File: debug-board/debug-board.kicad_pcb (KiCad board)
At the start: 2 copper layers, 29 parts, among them J14 Conn_01x02_Pin, J5 Conn_01x02_Pin, U1 AZ1117CH-3.3TRG1, U2 PIC18F47Q84-I/PT, U3 MAX3051ESA+, Y1 40MHz

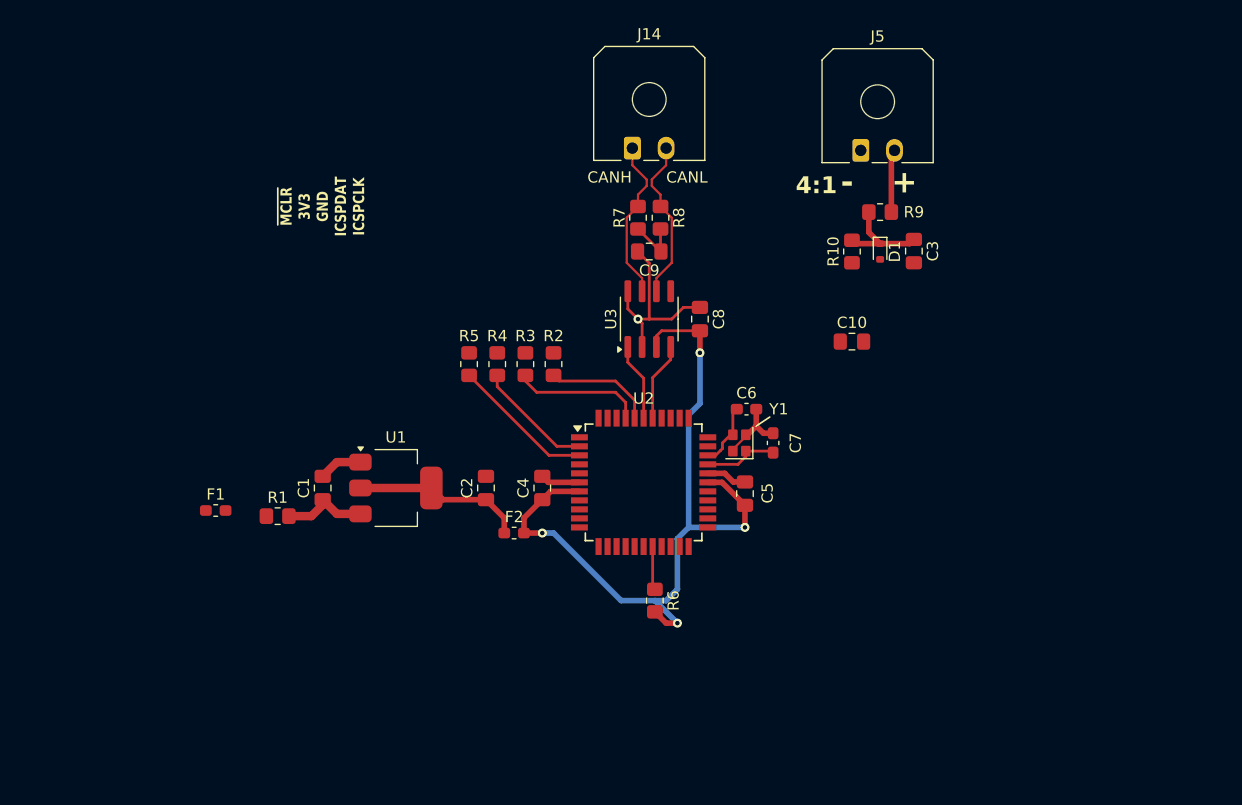
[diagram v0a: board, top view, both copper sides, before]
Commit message: Add a thermistor sensor and possibly connectors
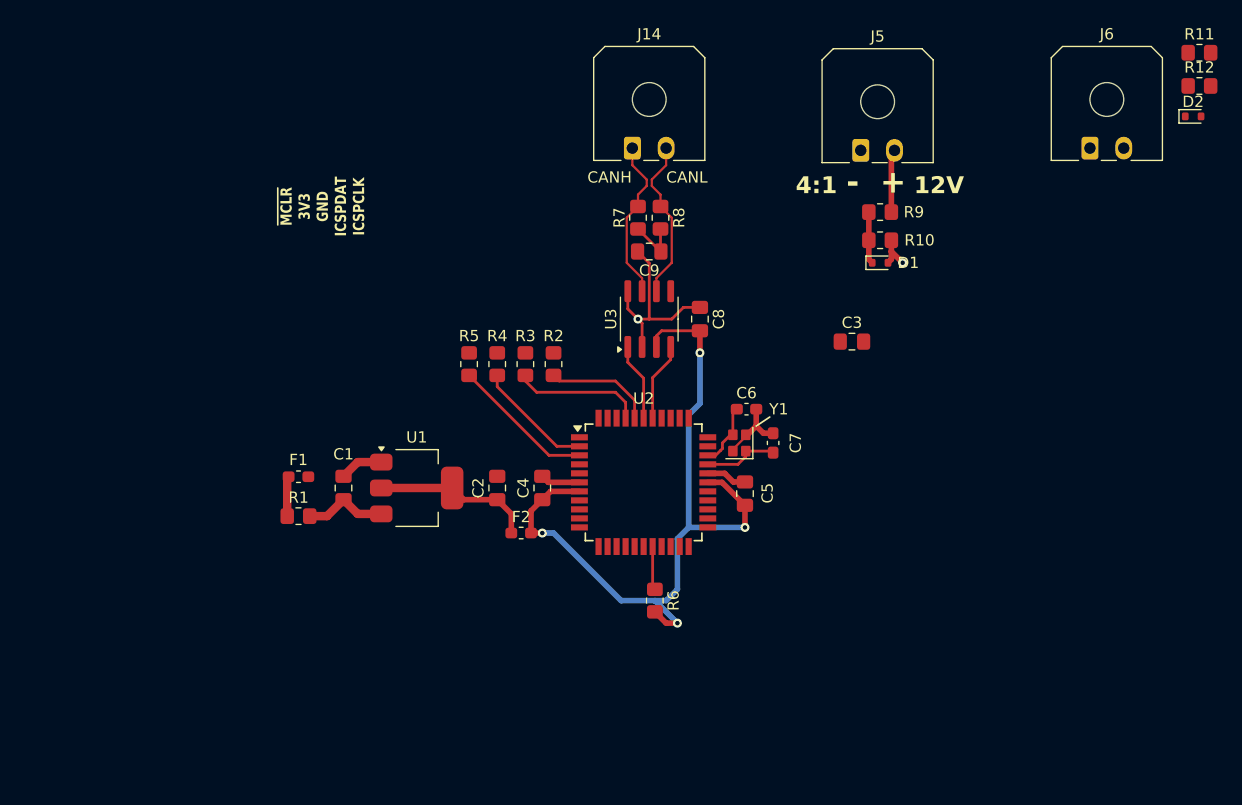
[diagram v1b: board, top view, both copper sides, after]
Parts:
- removed the C3 at (174.0, 79.5)
- added D2: BZT585B3V3T-7, Diode_SMD:D_SOD-523, F.Cu at (198.8, 67.5)
- added J6: Conn_01x02_Pin, Connector_Molex:Molex_Micro-Fit_3.0_43650-0200_1x02_P3.00mm_Horizontal, F.Cu at (189.6, 70.3)
- added R11: 40k, Resistor_SMD:R_0805_2012Metric_Pad1.20x1.40mm_HandSolder, F.Cu at (199.4, 61.9)
- added R12: 10k, Resistor_SMD:R_0805_2012Metric_Pad1.20x1.40mm_HandSolder, F.Cu at (199.4, 64.8)
- moved F1 7.94 mm to (119.3, 99.5), turned to 180 degrees
- moved R10 2.69 mm to (171.0, 78.5), turned to 180 degrees
- moved C1 1.85 mm to (123.3, 100.5)
- moved R1 1.85 mm to (119.3, 103.0)
- moved U1 1.85 mm to (129.8, 100.5)
- moved C2 1.00 mm to (137.0, 100.5)
- moved D1 1.00 mm to (171.0, 80.5), turned to 0 degrees
- moved F2 0.62 mm to (139.1, 104.5)
- renumbered C10 to C3
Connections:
- net /4:1 P/D renamed /4:1 P/D 1
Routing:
- net /4:1 P/D 1: track 8.99 -> 4.62 mm
- net Net-(F1-Pad2): track 0.00 -> 3.55 mm
- net GND: track 34.9 -> 38.5 mm, vias 1 -> 2
- net +3V3: track 68.9 -> 68.1 mm
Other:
- board text added: "12V"

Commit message: Changed footprint need to rearrange things
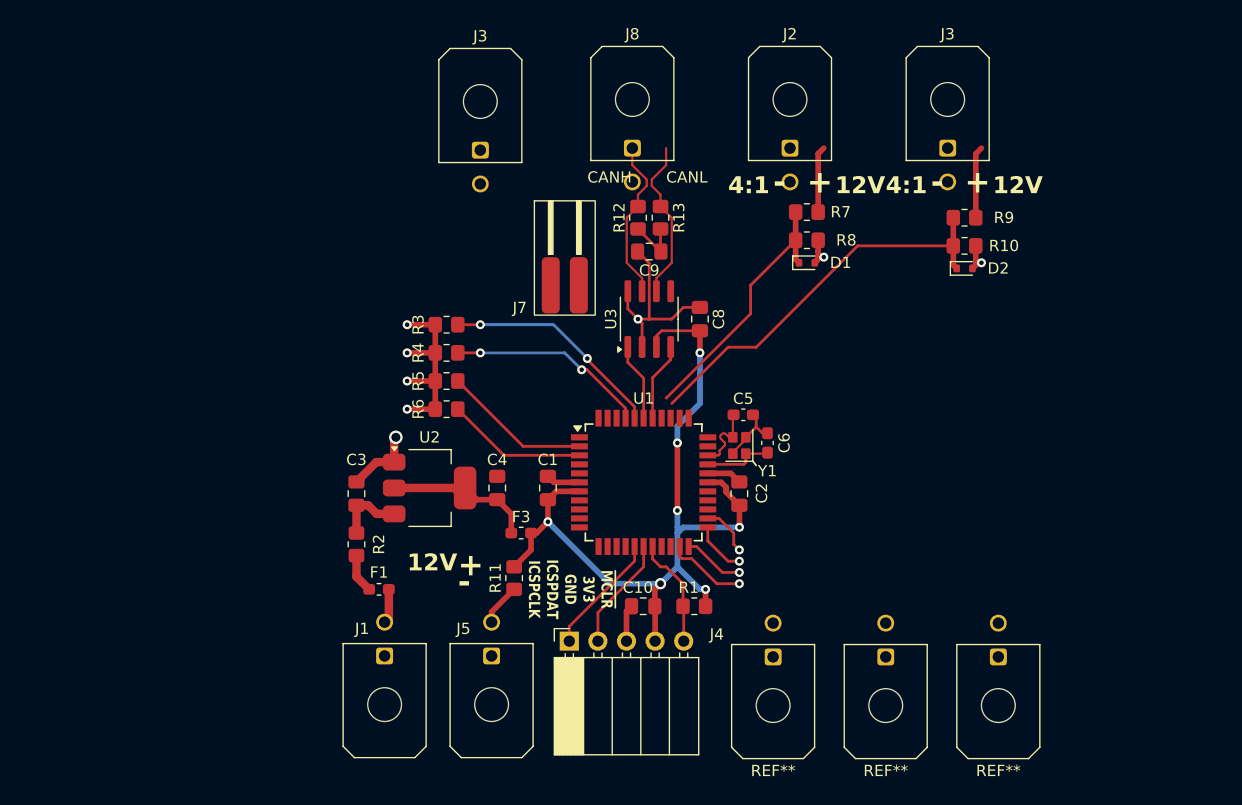
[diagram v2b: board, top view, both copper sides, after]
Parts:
- removed the C3 at (168.5, 87.5)
- added C10: 10u, Capacitor_SMD:C_0805_2012Metric_Pad1.18x1.45mm_HandSolder, F.Cu at (150.0, 111.0)
- added J1: Conn_01x02_Pin, Connector_Molex:Molex_Micro-Fit_3.0_43045-0200_2x01_P3.00mm_Horizontal, F.Cu at (127.0, 115.4)
- added J3: Conn_01x02_Pin, Connector_Molex:Molex_Micro-Fit_3.0_43045-0200_2x01_P3.00mm_Horizontal, F.Cu at (135.5, 70.5)
- added J4: Conn_01x05_Pin, Connector_PinSocket_2.54mm:PinSocket_1x05_P2.54mm_Horizontal, F.Cu at (143.4, 114.1)
- added J5: Conn_01x02_Pin, Connector_Molex:Molex_Micro-Fit_3.0_43045-0200_2x01_P3.00mm_Horizontal, F.Cu at (136.5, 115.4)
- added J7: Conn_01x02_Pin, sufst-lib:Conn2_SMD, F.Cu at (143.0, 82.5)
- added R11: 10k, Resistor_SMD:R_0805_2012Metric_Pad1.20x1.40mm_HandSolder, F.Cu at (138.5, 108.5)
- added REF**: Molex_Micro-Fit_3.0_43045-0200_2x01_P3.00mm_Horizontal, Connector_Molex:Molex_Micro-Fit_3.0_43045-0200_2x01_P3.00mm_Horizontal, F.Cu at (161.5, 115.5)
- added REF**: Molex_Micro-Fit_3.0_43045-0200_2x01_P3.00mm_Horizontal, Connector_Molex:Molex_Micro-Fit_3.0_43045-0200_2x01_P3.00mm_Horizontal, F.Cu at (181.5, 115.5)
- added REF**: Molex_Micro-Fit_3.0_43045-0200_2x01_P3.00mm_Horizontal, Connector_Molex:Molex_Micro-Fit_3.0_43045-0200_2x01_P3.00mm_Horizontal, F.Cu at (171.5, 115.5)
- J2: renamed from J5; footprint Connector_Molex:Molex_Micro-Fit_3.0_43650-0200_1x02_P3.00mm_Horizontal -> Connector_Molex:Molex_Micro-Fit_3.0_43045-0200_2x01_P3.00mm_Horizontal
- J3: renamed from J6; footprint Connector_Molex:Molex_Micro-Fit_3.0_43650-0200_1x02_P3.00mm_Horizontal -> Connector_Molex:Molex_Micro-Fit_3.0_43045-0200_2x01_P3.00mm_Horizontal
- J8: renamed from J14; footprint Connector_Molex:Molex_Micro-Fit_3.0_43650-0200_1x02_P3.00mm_Horizontal -> Connector_Molex:Molex_Micro-Fit_3.0_43045-0200_2x01_P3.00mm_Horizontal
- moved R9 25.5 mm to (178.5, 76.5)
- moved R10 25.2 mm to (178.5, 79.0), turned to 180 degrees
- moved D2 24.4 mm to (178.5, 81.0)
- moved J3 12.6 mm to (177.0, 70.3)
- moved F1 12.3 mm to (126.5, 109.5)
- moved R3 10.1 mm to (132.5, 86.0), turned to 180 degrees
- moved R4 7.07 mm to (132.5, 88.5), turned to 180 degrees
- moved D1 6.50 mm to (164.5, 80.5)
- moved R7 6.50 mm to (164.5, 76.0)
- moved R8 6.50 mm to (164.5, 78.5)
- moved J2 6.28 mm to (163.0, 70.3)
- moved R2 5.72 mm to (124.5, 105.5), turned to 90 degrees
- moved R5 4.74 mm to (132.5, 91.0), turned to 180 degrees
- moved R6 4.47 mm to (132.5, 93.5), turned to 180 degrees
- moved R1 3.54 mm to (154.5, 111.0), turned to 0 degrees
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- renumbered C4 to C1, C5 to C2, C1 to C3, C2 to C4, C6 to C5, C7 to C6, F2 to F3, R6 to R1, R12 to R10, R7 to R12, R8 to R13, R1 to R2, R2 to R3, R3 to R4, R4 to R5, R5 to R6, R9 to R7, R10 to R8, R11 to R9, U2 to U1, U1 to U2
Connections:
- net Net-(U2-RA6) renamed /CLK+
- net Net-(U2-RA7) renamed /CLK-
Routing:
- net /4:1 P/D 2: track 0.00 -> 35.4 mm
- net GND: track 38.5 -> 62.5 mm, vias 2 -> 8
- net /4:1 P/D 1: track 4.62 -> 23.4 mm
- net /ICSPCLK: track 0.00 -> 10.8 mm
- net /ICSPDAT: track 0.00 -> 10.1 mm
- net Net-(U1-RD2): track 9.71 -> 19.8 mm, vias 0 -> 2
- net unconnected-(U1-RA2-Pad21): track 0.00 -> 7.18 mm, vias 0 -> 1
- net Net-(J3-Pin_2): track 0.00 -> 6.39 mm
- net Net-(U1-RD3): track 11.6 -> 17.8 mm, vias 0 -> 2
- net /~{MCLR}: track 3.88 -> 9.84 mm
- net +3V3: track 68.1 -> 73.6 mm, vias 4 -> 7
- net unconnected-(U1-RA3-Pad22): track 0.00 -> 5.45 mm, vias 0 -> 1
- net unconnected-(U1-RA4-Pad23): track 0.00 -> 4.75 mm, vias 0 -> 1
- net unconnected-(U1-RA5-Pad24): track 0.00 -> 4.55 mm, vias 0 -> 1
- net /Sensor 1: track 0.00 -> 3.74 mm
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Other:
- board text removed: "${REFERENCE}"

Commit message: Changed connectors and added another thermistor
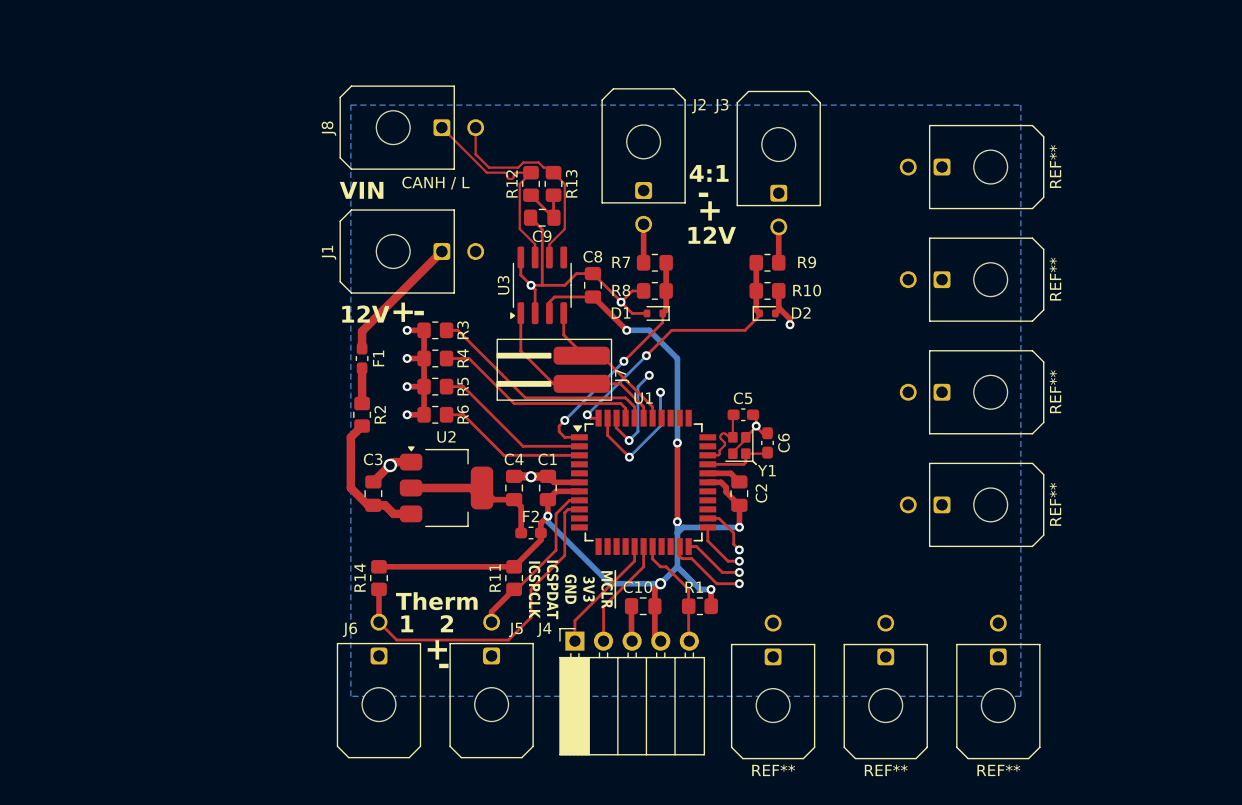
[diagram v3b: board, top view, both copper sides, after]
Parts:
- removed the J3 at (135.5, 70.5)
- added J6: Conn_01x02_Pin, Connector_Molex:Molex_Micro-Fit_3.0_43045-0200_2x01_P3.00mm_Horizontal, F.Cu at (126.5, 115.4)
- added R14: 10k, Resistor_SMD:R_0805_2012Metric_Pad1.20x1.40mm_HandSolder, F.Cu at (126.5, 108.5)
- added REF**: Molex_Micro-Fit_3.0_43045-0200_2x01_P3.00mm_Horizontal, Connector_Molex:Molex_Micro-Fit_3.0_43045-0200_2x01_P3.00mm_Horizontal, F.Cu at (176.5, 102.0)
- added REF**: Molex_Micro-Fit_3.0_43045-0200_2x01_P3.00mm_Horizontal, Connector_Molex:Molex_Micro-Fit_3.0_43045-0200_2x01_P3.00mm_Horizontal, F.Cu at (176.5, 92.0)
- added REF**: Molex_Micro-Fit_3.0_43045-0200_2x01_P3.00mm_Horizontal, Connector_Molex:Molex_Micro-Fit_3.0_43045-0200_2x01_P3.00mm_Horizontal, F.Cu at (176.5, 72.0)
- added REF**: Molex_Micro-Fit_3.0_43045-0200_2x01_P3.00mm_Horizontal, Connector_Molex:Molex_Micro-Fit_3.0_43045-0200_2x01_P3.00mm_Horizontal, F.Cu at (176.5, 82.0)
- moved J1 36.3 mm to (132.1, 79.5), turned to 90 degrees
- moved F1 20.6 mm to (125.0, 89.0), turned to -90 degrees
- moved D2 18.0 mm to (161.0, 85.0)
- moved R10 18.0 mm to (161.0, 83.0)
- moved R9 18.0 mm to (161.0, 80.5)
- moved J8 17.0 mm to (132.1, 68.5), turned to 90 degrees
- moved J3 15.5 mm to (162.0, 74.3)
- moved D1 14.2 mm to (151.0, 85.0), turned to 180 degrees
- moved R7 14.2 mm to (151.0, 80.5), turned to 180 degrees
- moved R8 14.2 mm to (151.0, 83.0), turned to 0 degrees
- moved J2 13.5 mm to (150.0, 74.1)
- moved R2 11.5 mm to (125.0, 94.0), turned to -90 degrees
- moved C8 9.96 mm to (145.5, 82.5)
- moved C9 9.96 mm to (141.0, 76.5)
- moved R12 9.96 mm to (140.0, 73.5)
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- renumbered F3 to F2
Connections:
- F1 pad 1: Net-(J1-Pin_2) -> Net-(J1-Pin_1)
- J1 pad 1: GND -> Net-(J1-Pin_1)
- J1 pad 2: Net-(J1-Pin_2) -> GND
- J5 pad 2: /Sensor 1 -> /Therm 2
- R11 pad 1: /Sensor 1 -> /Therm 2
- U1 pad 1: unconnected-(U1-RC7-Pad1) -> /4:1 P/D 1
- U1 pad 44: unconnected-(U1-RC6-Pad44) -> /4:1 P/D 2
- U1 pad 8: unconnected-(U1-RB0-Pad8) -> /Therm 2
- U1 pad 9: unconnected-(U1-RB1-Pad9) -> /Therm 1
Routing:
- net /Therm 1: track 0.00 -> 29.9 mm
- net +3V3: track 73.6 -> 93.0 mm
- net /Therm 2: track 0.00 -> 14.7 mm
- net Net-(J1-Pin_1): track 0.00 -> 11.6 mm
- net unconnected-(U1-RC5-Pad43): track 0.00 -> 11.2 mm, vias 0 -> 2
- net /4:1 P/D 2: track 35.4 -> 24.9 mm, vias 0 -> 2
- net /CAN_TX: track 7.04 -> 17.5 mm
- net unconnected-(U1-RC4-Pad42): track 0.00 -> 8.98 mm, vias 0 -> 2
- net /CAN_RX: track 7.12 -> 13.6 mm
- net +12V: track 6.13 -> 12.2 mm
- net /CAN-: track 14.5 -> 18.8 mm
- net /CAN+: track 14.5 -> 18.7 mm
- net GND: track 62.5 -> 66.6 mm, vias 8 -> 10
- net /Sensor 1: track 3.74 -> 0.00 mm
- net Net-(J3-Pin_2): track 6.39 -> 3.18 mm
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- added copper zone on B.Cu, net GND
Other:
- board text added: "1 2"
- board text added: "CANH / L"
- board text added: "Therm"
- board text added: "VIN"
- board text removed: "CANH"
- board text removed: "CANL"

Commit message: Rearrange board and change connector separation
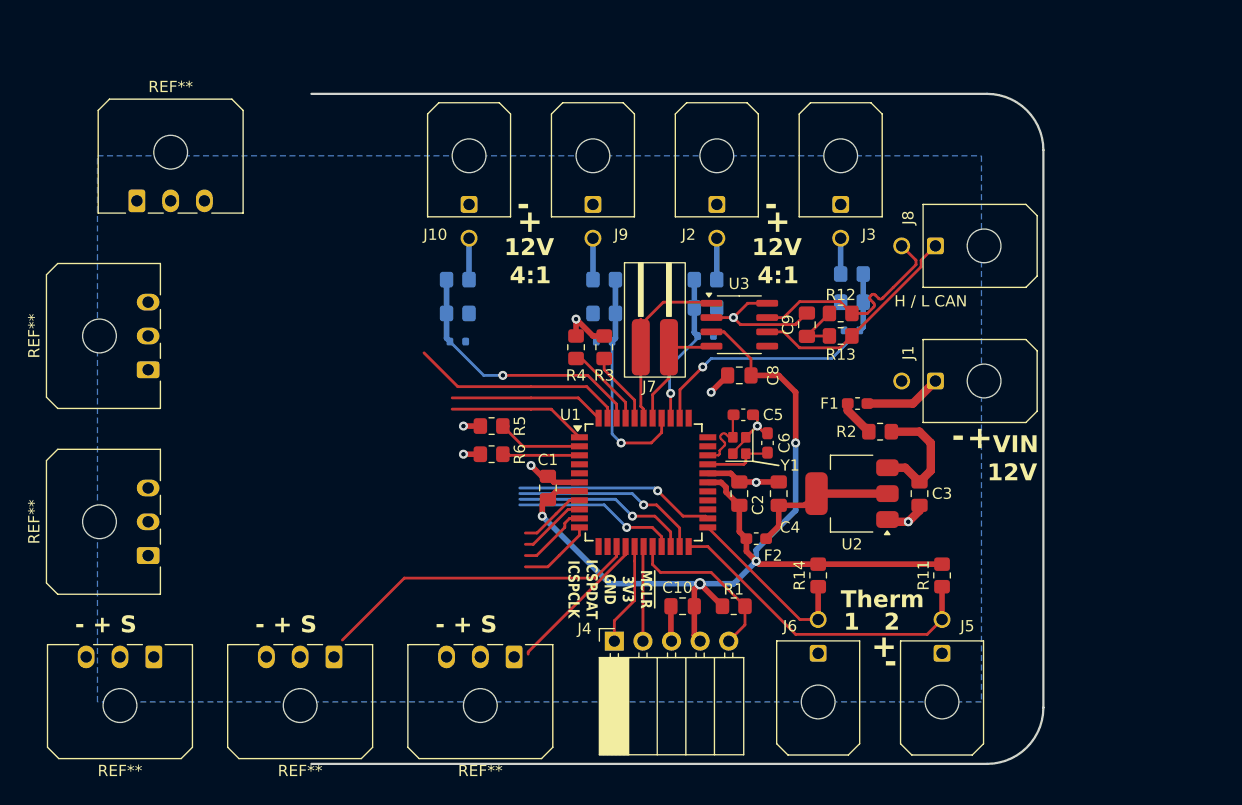
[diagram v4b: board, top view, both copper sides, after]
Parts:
- removed the REF** at (176.5, 102.0)
- removed the REF** at (161.5, 115.5)
- removed the REF** at (176.5, 92.0)
- removed the REF** at (181.5, 115.5)
- removed the REF** at (171.5, 115.5)
- removed the REF** at (176.5, 72.0)
- removed the REF** at (176.5, 82.0)
- added D3: BZT585B3V3T-7, Diode_SMD:D_SOD-523, B.Cu at (146.5, 87.5)
- added D4: BZT585B3V3T-7, Diode_SMD:D_SOD-523, B.Cu at (133.5, 87.5)
- added J10: Conn_01x02_Pin, Connector_Molex:Molex_Micro-Fit_3.0_43045-0200_2x01_P3.00mm_Horizontal, F.Cu at (134.5, 75.3)
- added J9: Conn_01x02_Pin, Connector_Molex:Molex_Micro-Fit_3.0_43045-0200_2x01_P3.00mm_Horizontal, F.Cu at (145.5, 75.3)
- added R15: 40k, Resistor_SMD:R_0805_2012Metric_Pad1.20x1.40mm_HandSolder, B.Cu at (146.5, 82.0)
- added R16: 10k, Resistor_SMD:R_0805_2012Metric_Pad1.20x1.40mm_HandSolder, B.Cu at (146.5, 85.0)
- added R17: 40k, Resistor_SMD:R_0805_2012Metric_Pad1.20x1.40mm_HandSolder, B.Cu at (133.5, 82.0)
- added R18: 10k, Resistor_SMD:R_0805_2012Metric_Pad1.20x1.40mm_HandSolder, B.Cu at (133.5, 85.0)
- added REF**: Molex_Micro-Fit_3.0_43650-0300_1x03_P3.00mm_Horizontal, Connector_Molex:Molex_Micro-Fit_3.0_43650-0300_1x03_P3.00mm_Horizontal, F.Cu at (106.0, 106.5)
- added REF**: Molex_Micro-Fit_3.0_43650-0300_1x03_P3.00mm_Horizontal, Connector_Molex:Molex_Micro-Fit_3.0_43650-0300_1x03_P3.00mm_Horizontal, F.Cu at (106.5, 115.5)
- added REF**: Molex_Micro-Fit_3.0_43650-0300_1x03_P3.00mm_Horizontal, Connector_Molex:Molex_Micro-Fit_3.0_43650-0300_1x03_P3.00mm_Horizontal, F.Cu at (106.0, 90.0)
- added REF**: Molex_Micro-Fit_3.0_43650-0300_1x03_P3.00mm_Horizontal, Connector_Molex:Molex_Micro-Fit_3.0_43650-0300_1x03_P3.00mm_Horizontal, F.Cu at (105.0, 75.0)
- added REF**: Molex_Micro-Fit_3.0_43650-0300_1x03_P3.00mm_Horizontal, Connector_Molex:Molex_Micro-Fit_3.0_43650-0300_1x03_P3.00mm_Horizontal, F.Cu at (122.5, 115.5)
- added REF**: Molex_Micro-Fit_3.0_43650-0300_1x03_P3.00mm_Horizontal, Connector_Molex:Molex_Micro-Fit_3.0_43650-0300_1x03_P3.00mm_Horizontal, F.Cu at (138.5, 115.5)
- D1, D2, R10, R7, R8, R9: moved to B.Cu
- moved C3 48.5 mm to (174.5, 101.0), turned to -90 degrees
- moved R2 46.0 mm to (171.0, 95.5), turned to 0 degrees
- moved J1 45.3 mm to (175.9, 91.0), turned to -90 degrees
- moved J8 45.1 mm to (175.9, 79.0), turned to -90 degrees
- moved F1 44.2 mm to (169.0, 93.0), turned to 180 degrees
- moved J5 40.0 mm to (176.5, 115.2)
- moved J6 39.0 mm to (165.5, 115.2)
- moved R14 39.0 mm to (165.5, 108.3)
- moved R11 38.0 mm to (176.5, 108.3)
- moved U2 36.0 mm to (168.5, 101.0), turned to 180 degrees
- moved R12 29.8 mm to (167.5, 85.0), turned to 0 degrees
- moved R13 28.9 mm to (167.5, 87.0), turned to 180 degrees
- moved C9 25.3 mm to (164.5, 86.0), turned to 90 degrees
- moved C4 23.5 mm to (162.0, 101.0)
- moved F2 20.0 mm to (160.0, 105.0), turned to 180 degrees
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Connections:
- J8 pad 1: /CAN+ -> /CAN-
- J8 pad 2: /CAN- -> /CAN+
- U1 pad 1: /4:1 P/D 1 -> unconnected-(U1-RC7-Pad1)
- U1 pad 22: unconnected-(U1-RA3-Pad22) -> /Therm 2
- U1 pad 23: unconnected-(U1-RA4-Pad23) -> /Therm 1
- U1 pad 35: unconnected-(U1-RC1-Pad35) -> /4:1 P/D 2
- U1 pad 36: unconnected-(U1-RC2-Pad36) -> /4:1 P/D 1
- U1 pad 37: unconnected-(U1-RC3-Pad37) -> /4:1 P/D 3
- U1 pad 42: unconnected-(U1-RC4-Pad42) -> /4:1 P/D 4
- U1 pad 44: /4:1 P/D 2 -> unconnected-(U1-RC6-Pad44)
- U1 pad 8: /Therm 2 -> unconnected-(U1-RB0-Pad8)
- U1 pad 9: /Therm 1 -> unconnected-(U1-RB1-Pad9)
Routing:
- net unconnected-(U1-RB4-Pad14): track 0.00 -> 28.3 mm
- net /4:1 P/D 4: track 0.00 -> 24.0 mm, vias 0 -> 1
- net /4:1 P/D 3: track 0.00 -> 20.2 mm, vias 0 -> 1
- net GND: track 66.6 -> 47.2 mm, vias 10 -> 9
- net unconnected-(U1-RA1-Pad20): track 0.00 -> 15.9 mm, vias 0 -> 1
- net unconnected-(U1-RA0-Pad19): track 0.00 -> 14.6 mm, vias 0 -> 1
- net /Therm 2: track 14.7 -> 29.2 mm
- net Net-(U1-RD2): track 21.0 -> 6.92 mm
- net /Therm 1: track 29.9 -> 16.1 mm
- net unconnected-(U1-RC6-Pad44): track 0.00 -> 13.7 mm
- net unconnected-(U1-RA5-Pad24): track 4.55 -> 17.8 mm
- net unconnected-(U1-RB5-Pad15): track 0.00 -> 13.1 mm
- net unconnected-(U1-RC7-Pad1): track 0.00 -> 12.3 mm
- net Net-(U1-RD3): track 18.6 -> 7.42 mm
- net unconnected-(U1-RA2-Pad21): track 7.18 -> 17.1 mm
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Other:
- board outline added: 65 x 59.5 mm
- board text added: "- + S"
- board text added: "H / L CAN"
- board text removed: "CANH / L"
